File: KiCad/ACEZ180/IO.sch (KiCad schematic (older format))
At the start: 13 parts, among them Q500 2N3904, U2 Z84C20, X3 CRYSTALHC49U-V 10Mhz

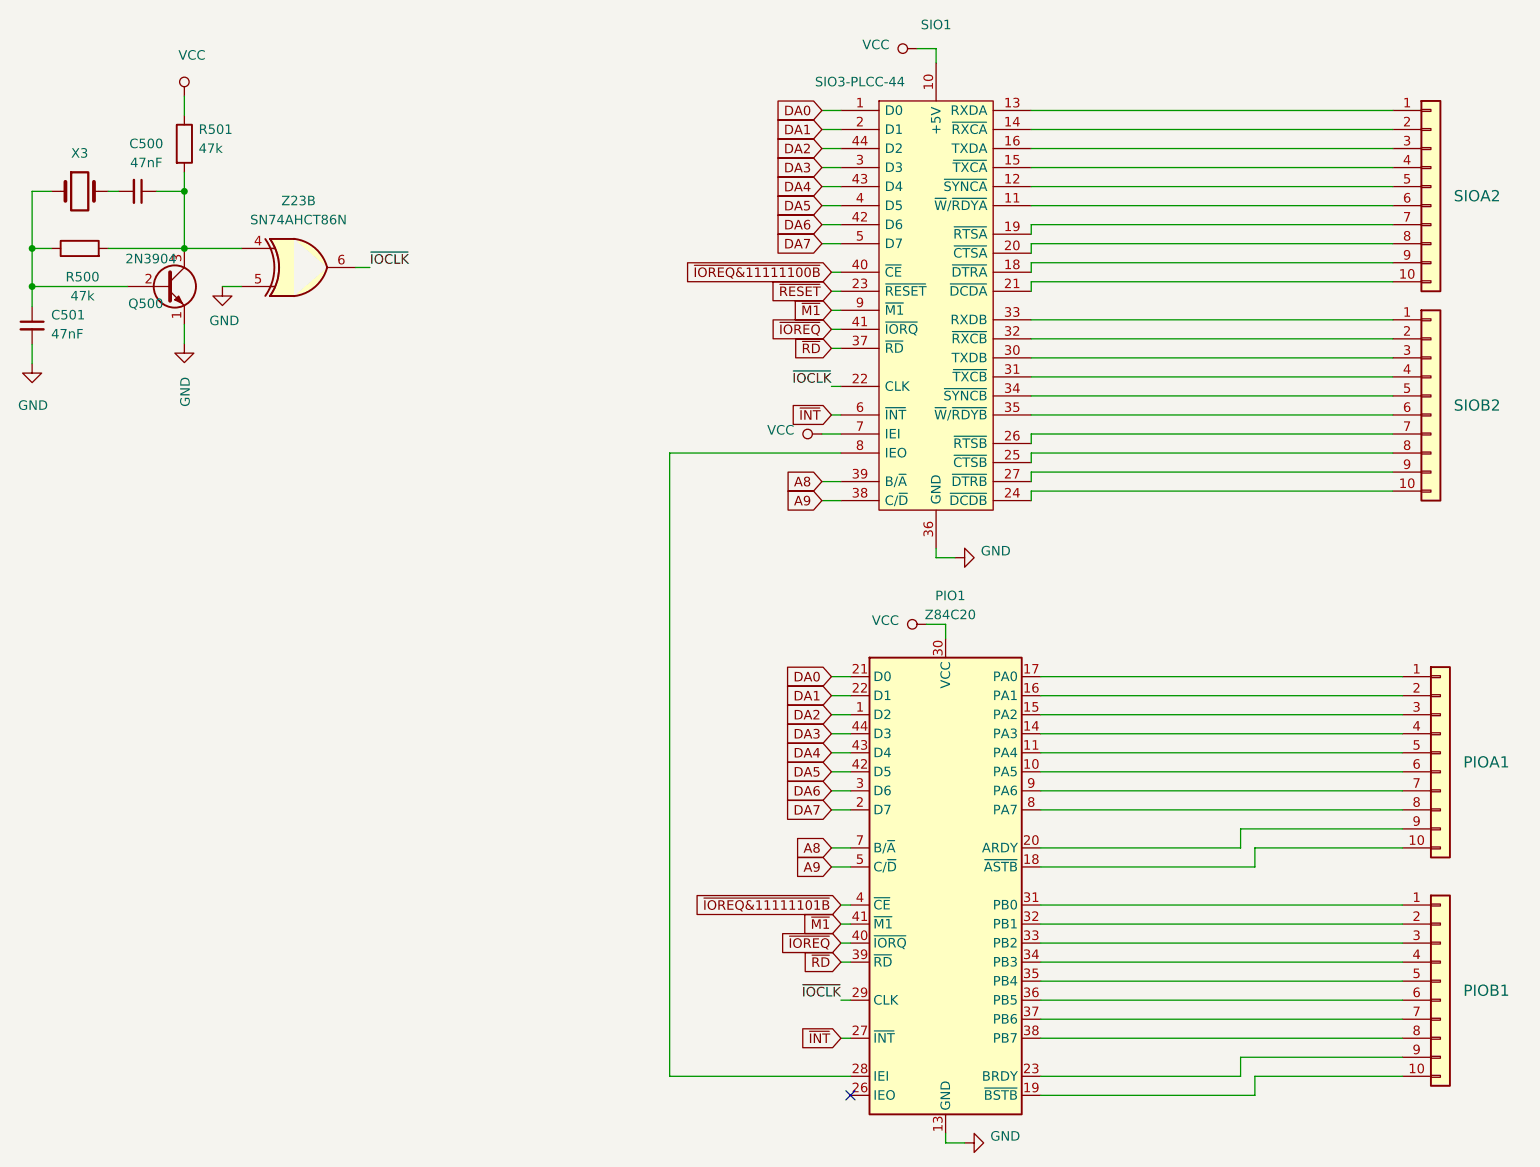
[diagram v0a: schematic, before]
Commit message: Move Towards Ac3 test board, include KIO chip, regaranged port selection, ROM exapsion to 3000-3FFF relocated base of RAM to 4000 and inrease RAM to 48k. Change 40Hz interupt to work via CLK/TRG3 so the IM can be changed to use IM 2. This will require updated ROM.
Signed-off-by: John Bradley <flypie@rocketmail.com>
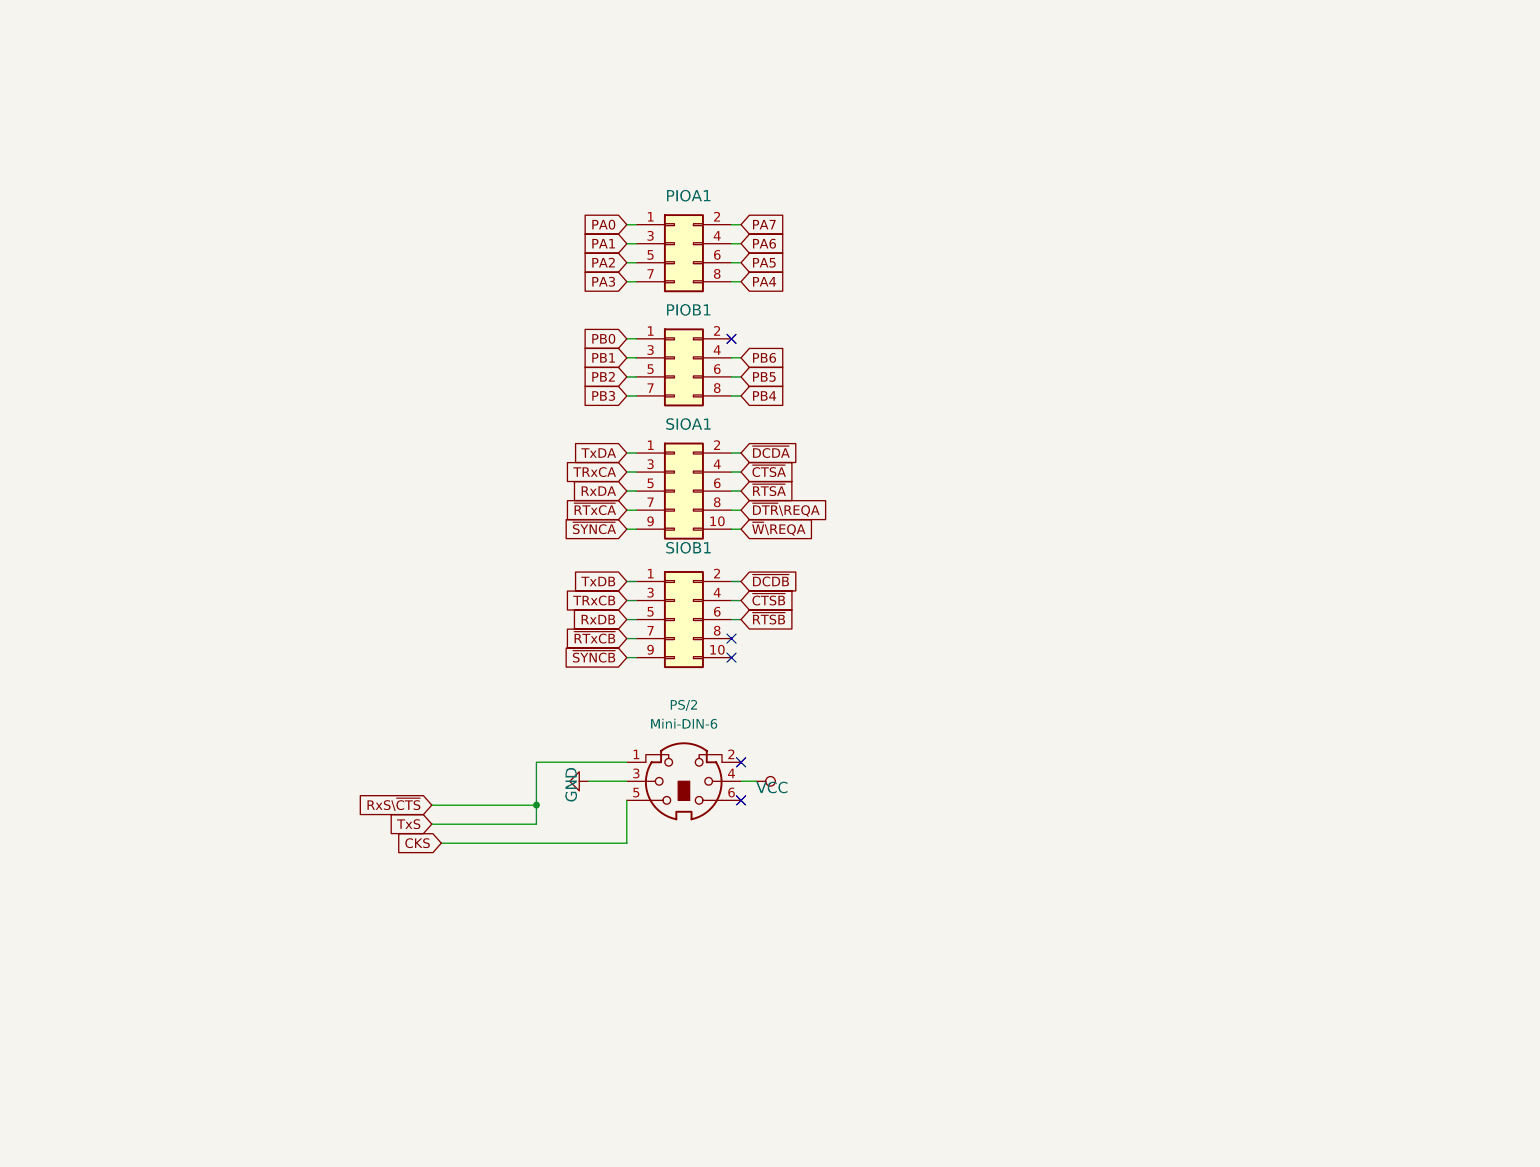
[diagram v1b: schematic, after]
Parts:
- removed C500, C501: 47nF, Capacitor_THT:C_Disc_D5.0mm_W2.5mm_P5.00mm, symbol Device:C_Small
- removed PIOA1, PIOB1, SIOA2, SIOB2: 2510-, Connector_PinHeader_2.54mm:PinHeader_2x05_P2.54mm_Vertical, symbol Connector_Generic:Conn_01x10
- removed Q500: 2N3904, Package_TO_SOT_THT:TO-92_Inline, symbol Transistor_BJT:2N3904
- removed R500, R501: 47k, Resistor_THT:R_Axial_DIN0204_L3.6mm_D1.6mm_P1.90mm_Vertical, symbol Device:R
- removed SIO1: SIO3-PLCC-44, Package_LCC:PLCC-44_THT-Socket, symbol Zilog_Z80_Peripherals:SIO3-PLCC-44
- removed U2: Z84C20, Package_LCC:PLCC-44_THT-Socket, symbol Zilog_Z80_Peripherals:PIO-PLCC-44
- removed X3: CRYSTALHC49U-V 10Mhz, Crystal:Crystal_HC49-U_Vertical, symbol Device:Crystal
- removed Z23: SN74AHCT86N, Package_DIP:DIP-14_W7.62mm, symbol 74xx:74LS86
- added PIOA1, PIOB1: 2510-, Connector_PinHeader_2.54mm:PinHeader_2x04_P2.54mm_Vertical, symbol Connector_Generic:Conn_02x04_Odd_Even
- added PS/2: Mini-DIN-6, Local:5749180-1, symbol Connector:Mini-DIN-6
- added SIOA1, SIOB1: 2510-, Connector_PinHeader_2.54mm:PinHeader_2x05_P2.54mm_Vertical, symbol Connector_Generic:Conn_02x05_Odd_Even
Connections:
- net GND: now also PS/2.3
- net VCC: now also PS/2.4
- new net CKS: PS/2.5
- new net PA0: PIOA1.1 (Pin_1)
- new net PA1: PIOA1.3 (Pin_3)
- new net PA2: PIOA1.5 (Pin_5)
- new net PA3: PIOA1.7 (Pin_7)
- new net PA4: PIOA1.8 (Pin_8)
- new net PA5: PIOA1.6 (Pin_6)
- new net PA6: PIOA1.4 (Pin_4)
- new net PA7: PIOA1.2 (Pin_2)
- new net PB0: PIOB1.1 (Pin_1)
- new net PB1: PIOB1.3 (Pin_3)
- new net PB2: PIOB1.5 (Pin_5)
- new net PB3: PIOB1.7 (Pin_7)
- new net PB4: PIOB1.8 (Pin_8)
- new net PB5: PIOB1.6 (Pin_6)
- new net PB6: PIOB1.4 (Pin_4)
- new net RxDA: SIOA1.5 (Pin_5)
- new net RxDB: SIOB1.5 (Pin_5)
- new net RxS\~CTS~: PS/2.1
- new net TRxCA: SIOA1.3 (Pin_3)
- new net TRxCB: SIOB1.3 (Pin_3)
- new net TxDA: SIOA1.1 (Pin_1)
- new net TxDB: SIOB1.1 (Pin_1)
- new net ~CTSA: SIOA1.4 (Pin_4)
- new net ~CTSB: SIOB1.4 (Pin_4)
- new net ~DCDA: SIOA1.2 (Pin_2)
- new net ~DCDB: SIOB1.2 (Pin_2)
- new net ~DTR~\REQA: SIOA1.8 (Pin_8)
- new net ~RTSA: SIOA1.6 (Pin_6)
- new net ~RTSB: SIOB1.6 (Pin_6)
- new net ~RTxCA: SIOA1.7 (Pin_7)
- new net ~RTxCB: SIOB1.7 (Pin_7)
- new net ~SYNCA: SIOA1.9 (Pin_9)
- new net ~SYNCB: SIOB1.9 (Pin_9)
- new net ~W~\REQA: SIOA1.10 (Pin_10)
- no-connect marks 1 -> 5
